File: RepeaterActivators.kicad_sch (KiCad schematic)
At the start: 63 parts, among them J1 AudioJack1_Grounded, J2 AudioJack2_Grounded, J3 Conn_01x05_Female, J4 8PRJ45_LED_Shielded_Radio1, J5 8PRJ45_LED_Shielded_Radio2, J6 Conn_01x02_Female, J7 Conn_01x02_Female, J8 Conn_01x02_Female, Q1 2N7000, Q2 2N7000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

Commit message: DBD: positioning components on the board
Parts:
- added H1, H2, H3, H4: MountingHole, MountingHole:MountingHole_2.7mm_M2.5, symbol Mechanical:MountingHole
- J3: footprint (none) -> Connector_PinSocket_2.00mm:PinSocket_1x05_P2.00mm_Horizontal
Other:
- note added: "Mounting Holes"
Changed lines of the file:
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@@
   (junction (at 238.76 241.3) (diameter 0) (color 0 0 0 0)
   )
-  (junction (at 229.87 179.07) (diameter 0) (color 0 0 0 0)
-  )
   (junction (at 173.99 204.47) (diameter 0) (color 0 0 0 0)
   )
@@
   (junction (at 217.17 168.91) (diameter 0) (color 0 0 0 0)
   )
+  (junction (at 226.06 212.09) (diameter 0) (color 0 0 0 0)
+  )
   (junction (at 356.87 147.32) (diameter 0) (color 0 0 0 0)
   )
@@
     (stroke (width 0) (type default) (color 0 0 0 0))
   )
-  (wire (pts (xy 238.76 236.22) (xy 229.87 236.22))
+  (wire (pts (xy 226.06 236.22) (xy 238.76 236.22))
     (stroke (width 0) (type default) (color 0 0 0 0))
   )
@@
     (stroke (width 0) (type default) (color 0 0 0 0))
   )
+  (polyline (pts (xy 95.25 280.67) (xy 69.85 280.67))
+    (stroke (width 0) (type default) (color 0 0 0 0))
+  )
   (wire (pts (xy 326.39 252.73) (xy 358.14 252.73))
     (stroke (width 0) (type default) (color 0 0 0 0))
@@
     (stroke (width 0) (type default) (color 0 0 0 0))
   )
-  (wire (pts (xy 229.87 236.22) (xy 229.87 179.07))
-    (stroke (width 0) (type default) (color 0 0 0 0))
-  )
   (wire (pts (xy 356.87 234.95) (xy 358.14 234.95))
     (stroke (width 0) (type default) (color 0 0 0 0))
@@
     (stroke (width 0) (type default) (color 0 0 0 0))
   )
-  (wire (pts (xy 226.06 179.07) (xy 229.87 179.07))
+  (wire (pts (xy 226.06 179.07) (xy 236.22 179.07))
     (stroke (width 0) (type default) (color 0 0 0 0))
   )
@@
     (stroke (width 0) (type default) (color 0 0 0 0))
   )
+  (wire (pts (xy 226.06 212.09) (xy 226.06 236.22))
+    (stroke (width 0) (type default) (color 0 0 0 0))
+  )
   (wire (pts (xy 283.21 205.74) (xy 295.91 205.74))
     (stroke (width 0) (type default) (color 0 0 0 0))
@@
     (stroke (width 0) (type default) (color 0 0 0 0))
   )
+  (polyline (pts (xy 69.85 241.3) (xy 95.25 241.3))
+    (stroke (width 0) (type default) (color 0 0 0 0))
+  )
   (wire (pts (xy 373.38 142.24) (xy 387.35 142.24))
     (stroke (width 0) (type default) (color 0 0 0 0))
@@
     (stroke (width 0) (type default) (color 0 0 0 0))
   )
-  (wire (pts (xy 213.36 179.07) (xy 226.06 179.07))
+  (polyline (pts (xy 95.25 241.3) (xy 95.25 280.67))
     (stroke (width 0) (type default) (color 0 0 0 0))
   )
-  (wire (pts (xy 229.87 179.07) (xy 236.22 179.07))
+  (wire (pts (xy 213.36 179.07) (xy 226.06 179.07))
     (stroke (width 0) (type default) (color 0 0 0 0))
   )
@@
     (stroke (width 0) (type default) (color 0 0 0 0))
   )
+  (polyline (pts (xy 69.85 241.3) (xy 69.85 280.67))
+    (stroke (width 0) (type default) (color 0 0 0 0))
+  )
   (wire (pts (xy 236.22 177.8) (xy 238.76 177.8))
     (stroke (width 0) (type default) (color 0 0 0 0))
@@
     (effects (font (size 1.27 1.27)) (justify left bottom))
   )
+  (text "Mounting Holes" (at 69.85 241.3 0)
+    (effects (font (size 1.27 1.27)) (justify left bottom))
+  )
   (text "This should allow for ~53KHz signals to pass through."
     (at 110.49 297.18 0)
@@
     (pin "1")
   )
+  (symbol (lib_id "Mechanical:MountingHole") (at 74.93 257.81 0) (unit 1)
+    (in_bom yes) (on_board yes) (fields_autoplaced)
+    (property "Reference" "H2" (id 0) (at 77.47 256.9753 0)
+      (effects (font (size 1.27 1.27)) (justify left))
+    )
+    (property "Value" "MountingHole" (id 1) (at 77.47 259.5122 0)
+      (effects (font (size 1.27 1.27)) (justify left))
+    )
+    (property "Footprint" "MountingHole:MountingHole_2.7mm_M2.5" (id 2) (at 74.93 257.81 0)
+      (effects (font (size 1.27 1.27)) hide)
+    )
+    (property "Datasheet" "~" (id 3) (at 74.93 257.81 0)
+      (effects (font (size 1.27 1.27)) hide)
+    )
+  )
   (symbol (lib_id "Diode:1N4001") (at 356.87 295.91 180) (unit 1)
     (in_bom yes) (on_board yes) (fields_autoplaced)
@@
     (property "Reference" "J3" (id 0) (at 127.635 135.543 0))
     (property "Value" "Conn_01x05_Female" (id 1) (at 127.635 138.0799 0))
-    (property "Footprint" "" (id 2) (at 127 144.78 0)
+    (property "Footprint" "Connector_PinSocket_2.00mm:PinSocket_1x05_P2.00mm_Horizontal" (id 2) (at 127 144.78 0)
       (effects (font (size 1.27 1.27)) hide)
     )
@@
     (pin "2")
   )
+  (symbol (lib_id "Mechanical:MountingHole") (at 74.93 275.59 0) (unit 1)
+    (in_bom yes) (on_board yes) (fields_autoplaced)
+    (property "Reference" "H4" (id 0) (at 77.47 274.7553 0)
+      (effects (font (size 1.27 1.27)) (justify left))
+    )
+    (property "Value" "MountingHole" (id 1) (at 77.47 277.2922 0)
+      (effects (font (size 1.27 1.27)) (justify left))
+    )
+    (property "Footprint" "MountingHole:MountingHole_2.7mm_M2.5" (id 2) (at 74.93 275.59 0)
+      (effects (font (size 1.27 1.27)) hide)
+    )
+    (property "Datasheet" "~" (id 3) (at 74.93 275.59 0)
+      (effects (font (size 1.27 1.27)) hide)
+    )
+  )
   (symbol (lib_id "power:GND") (at 173.99 217.17 0) (unit 1)
     (in_bom yes) (on_board yes) (fields_autoplaced)
@@
     (pin "3")
   )
+  (symbol (lib_id "Mechanical:MountingHole") (at 74.93 248.92 0) (unit 1)
+    (in_bom yes) (on_board yes) (fields_autoplaced)
+    (property "Reference" "H1" (id 0) (at 77.47 248.0853 0)
+      (effects (font (size 1.27 1.27)) (justify left))
+    )
+    (property "Value" "MountingHole" (id 1) (at 77.47 250.6222 0)
+      (effects (font (size 1.27 1.27)) (justify left))
+    )
+    (property "Footprint" "MountingHole:MountingHole_2.7mm_M2.5" (id 2) (at 74.93 248.92 0)
+      (effects (font (size 1.27 1.27)) hide)
+    )
+    (property "Datasheet" "~" (id 3) (at 74.93 248.92 0)
+      (effects (font (size 1.27 1.27)) hide)
+    )
+  )
   (symbol (lib_id "power:GND") (at 251.46 190.5 0) (unit 1)
     (in_bom yes) (on_board yes) (fields_autoplaced)
@@
     (pin "3")
   )
+  (symbol (lib_id "Mechanical:MountingHole") (at 74.93 266.7 0) (unit 1)
+    (in_bom yes) (on_board yes) (fields_autoplaced)
+    (property "Reference" "H3" (id 0) (at 77.47 265.8653 0)
+      (effects (font (size 1.27 1.27)) (justify left))
+    )
+    (property "Value" "MountingHole" (id 1) (at 77.47 268.4022 0)
+      (effects (font (size 1.27 1.27)) (justify left))
+    )
+    (property "Footprint" "MountingHole:MountingHole_2.7mm_M2.5" (id 2) (at 74.93 266.7 0)
+      (effects (font (size 1.27 1.27)) hide)
+    )
+    (property "Datasheet" "~" (id 3) (at 74.93 266.7 0)
+      (effects (font (size 1.27 1.27)) hide)
+    )
+  )
   (symbol (lib_id "power:+12V") (at 87.63 63.5 180) (unit 1)
     (in_bom yes) (on_board yes) (fields_autoplaced)
@@
       (reference "FB1") (unit 1) (value "FerriteBead") (footprint "Inductor_SMD:L_0603_1608Metric")
     )
+    (path "/cd7a2035-243b-43f2-8c9f-230f31a20a86"
+      (reference "H1") (unit 1) (value "MountingHole") (footprint "MountingHole:MountingHole_2.7mm_M2.5")
+    )
+    (path "/3489b7cc-d918-4b71-816e-4aaff6acd37e"
+      (reference "H2") (unit 1) (value "MountingHole") (footprint "MountingHole:MountingHole_2.7mm_M2.5")
+    )
+    (path "/ff7fecd6-8a9c-4240-a4fb-49c977dfa830"
+      (reference "H3") (unit 1) (value "MountingHole") (footprint "MountingHole:MountingHole_2.7mm_M2.5")
+    )
+    (path "/a9a6de20-e5eb-4ae9-add8-fed8143ee40e"
+      (reference "H4") (unit 1) (value "MountingHole") (footprint "MountingHole:MountingHole_2.7mm_M2.5")
+    )
     (path "/5a0f2744-b455-4140-94c0-9bae6263664f"
       (reference "J1") (unit 1) (value "AudioJack1_Grounded") (footprint "Connector_Audio:Jack_3.5mm_CUI_SJ-3523-SMT_Horizontal")
@@
     )
     (path "/9bc6aedf-ba78-468a-91bb-e5cb92017a01"
-      (reference "J3") (unit 1) (value "Conn_01x05_Female") (footprint "")
+      (reference "J3") (unit 1) (value "Conn_01x05_Female") (footprint "Connector_PinSocket_2.00mm:PinSocket_1x05_P2.00mm_Horizontal")
     )
     (path "/0e8893fe-7c69-4208-b877-cdaf89618e50"

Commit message: DBD: Removed RC and added delayed start 555 IC for MR on 273 due to discoveries in breadboarding
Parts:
- removed Q9: 2N7000, Package_TO_SOT_THT:TO-92_Inline, symbol Transistor_FET:2N7000
- added C? (x7): 0.1u, Capacitor_THT:C_Disc_D3.4mm_W2.1mm_P2.50mm, symbol Device:C
- added D?: 15V/5W, symbol Device:D_Zener
- added Q?: 2N7000, Package_TO_SOT_THT:TO-92_Inline, symbol Transistor_FET:2N7000
- added U?: LM555xM, Package_SO:SOIC-8_3.9x4.9mm_P1.27mm, symbol Timer:LM555xM
- C5: value 100m -> 47u
- R17, R18: value 500 -> 10k
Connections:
- net +12V: now also D?.1 (K)
- net +5V: now also C?.1, C?.1, C?.1, C?.1, C?.1, C?.1, C?.2
- net GND: now also R18.2, C?.1, C?.2, C?.2, C?.2, C?.2, C?.2, C?.2, D?.2 (A), Q?.1 (S), U?.1 (GND)
- net at R18.1: now also C5.1, U?.2 (TR), U?.6 (THR); no longer D1.2 (A)
- net at D1.1 (K): now also Q?.2 (G)
- net at R17.2, U2.1 (~{Mr}): now also Q?.3 (D)
- net at C5.2, U2.19 (Q7), U3.6 (E3)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: now also U?.8 (VCC)
- new net: D1.2 (A), U?.3 (Q)
- no-connect marks 16 -> 19
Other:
- note added: "A decoupling (or bypass) capacitor in close proximity to every IC's power pin provides transient current when switching between logic levels."
- note added: "Zener diode protects circuit against reverse current"
- moved on the sheet: C2, C3, C5, D1, H1, H2, H3, H4, J1, J2, J8, R1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

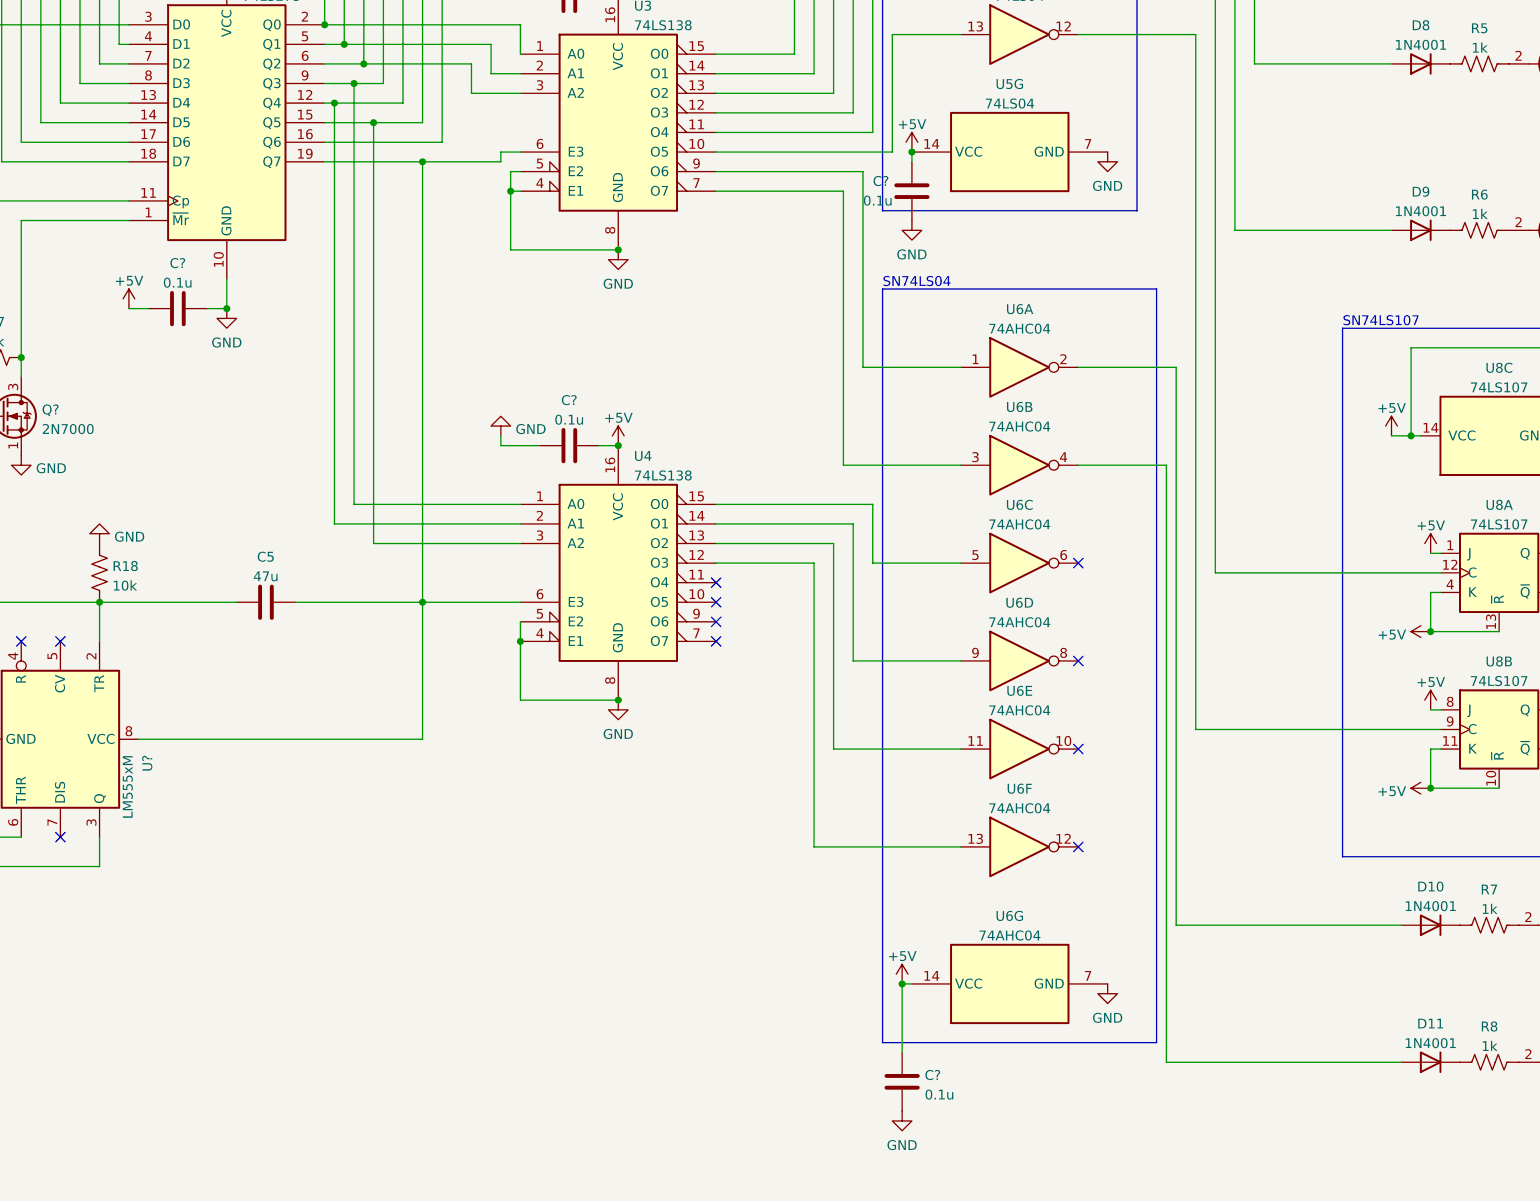
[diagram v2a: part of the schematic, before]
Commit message: DBD: demux activation fix
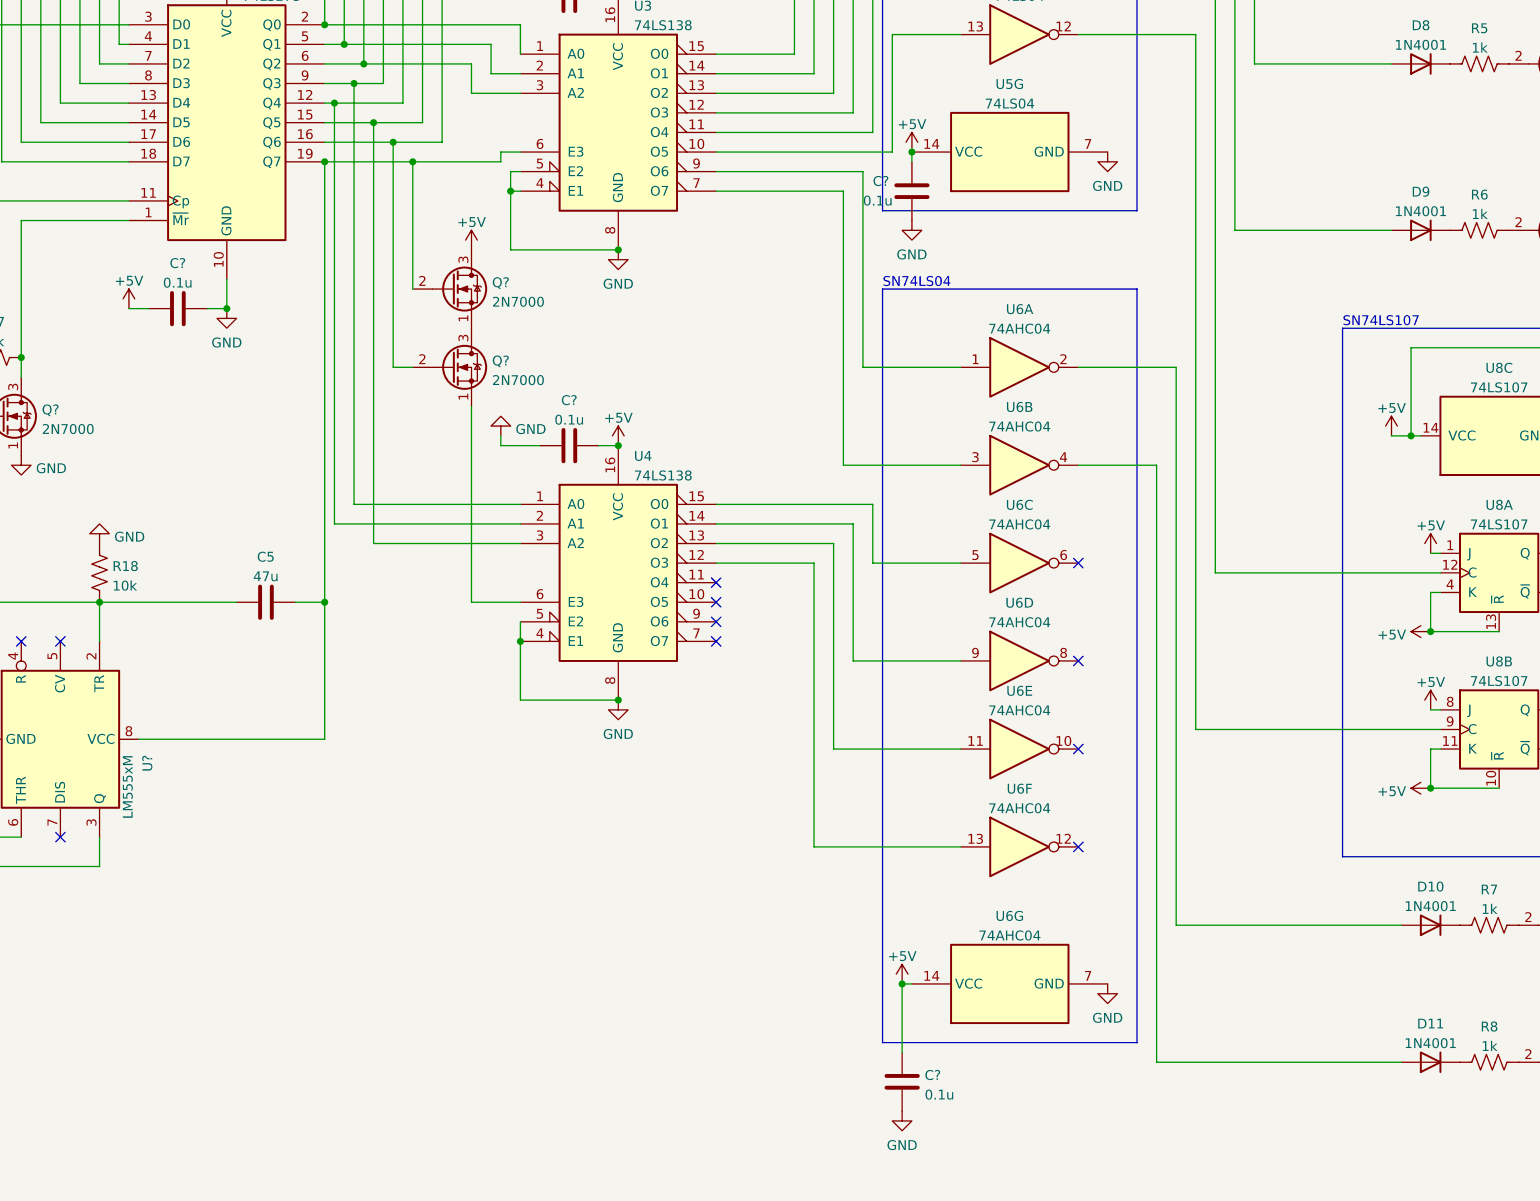
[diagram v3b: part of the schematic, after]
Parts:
- added Q? (x2): 2N7000, Package_TO_SOT_THT:TO-92_Inline, symbol Transistor_FET:2N7000
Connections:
- net +5V: now also Q?.3 (D)
- net at C5.2, U2.19 (Q7), U3.6 (E3)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: now also Q?.2 (G); no longer U4.6 (E3)
- net at U2.16 (Q6), U2.18 (D7): now also Q?.2 (G)
- new net: Q?.1 (S), U4.6 (E3)
- new net: Q?.1 (S), Q?.3 (D)
